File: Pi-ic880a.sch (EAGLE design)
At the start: 20 parts, among them Q1 LFXTAL016178, U1 IC880A, U2 BR24G32-3, U3 MCP79412-I/SN

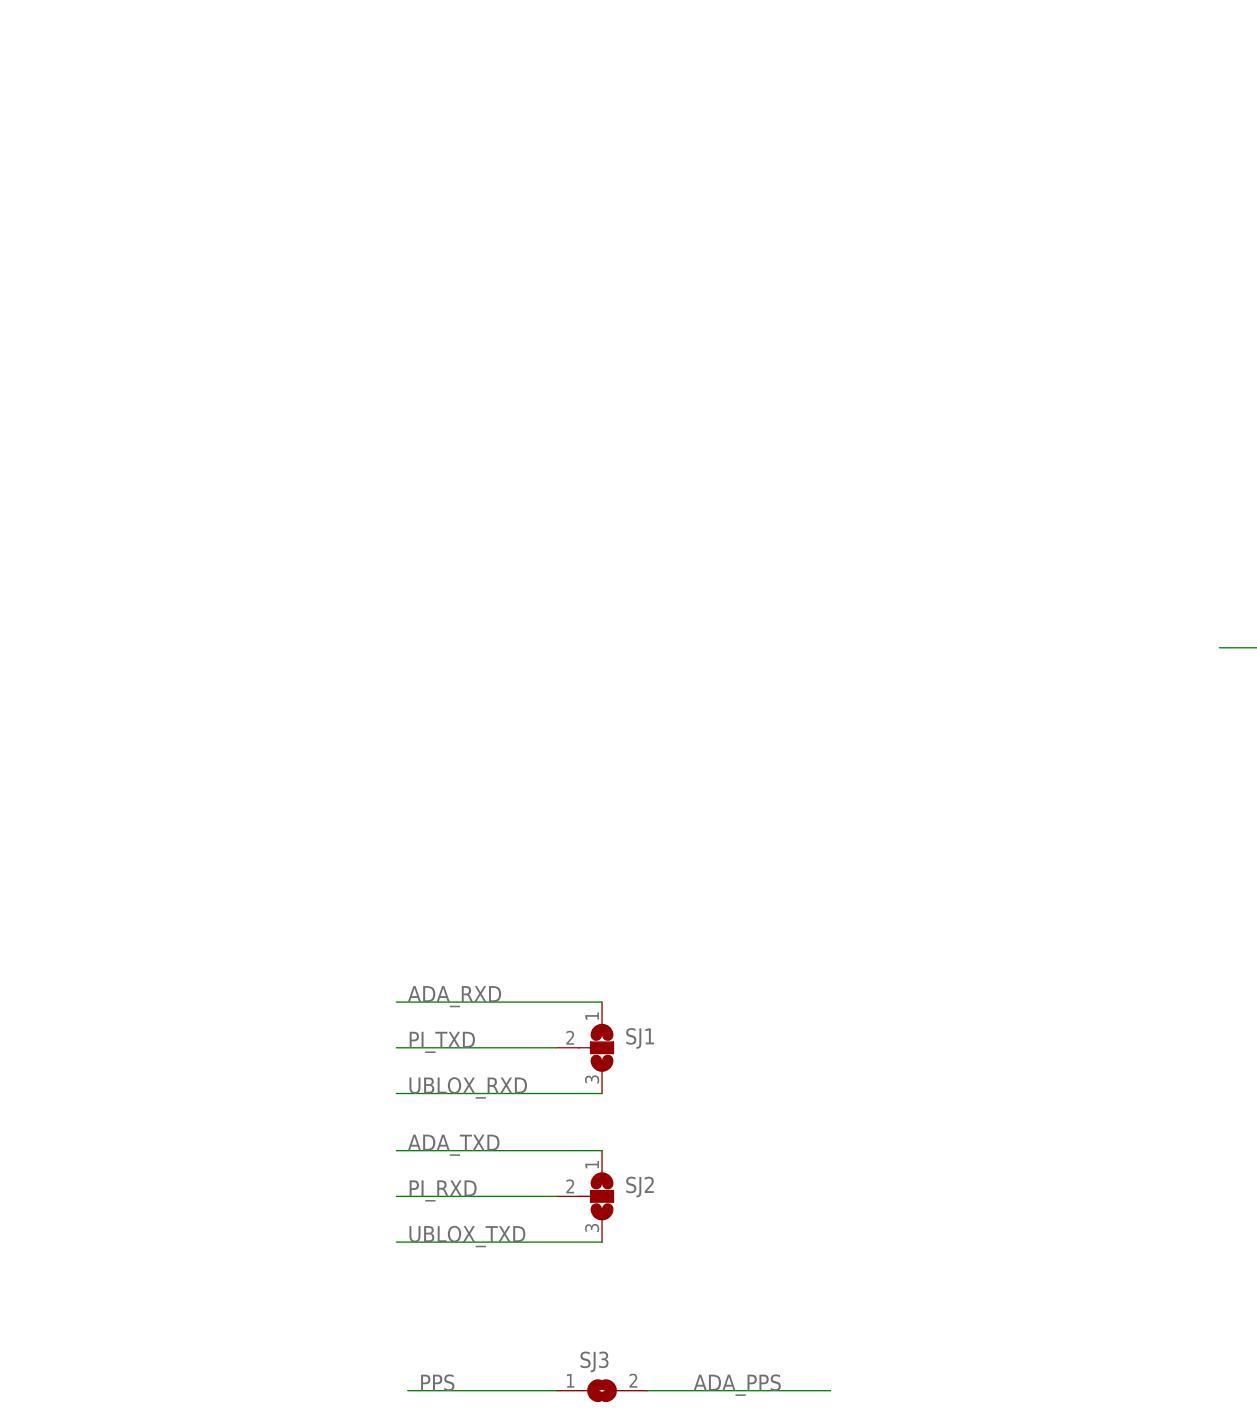
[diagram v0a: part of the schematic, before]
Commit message: Standalone version of the adafruit GPS module added
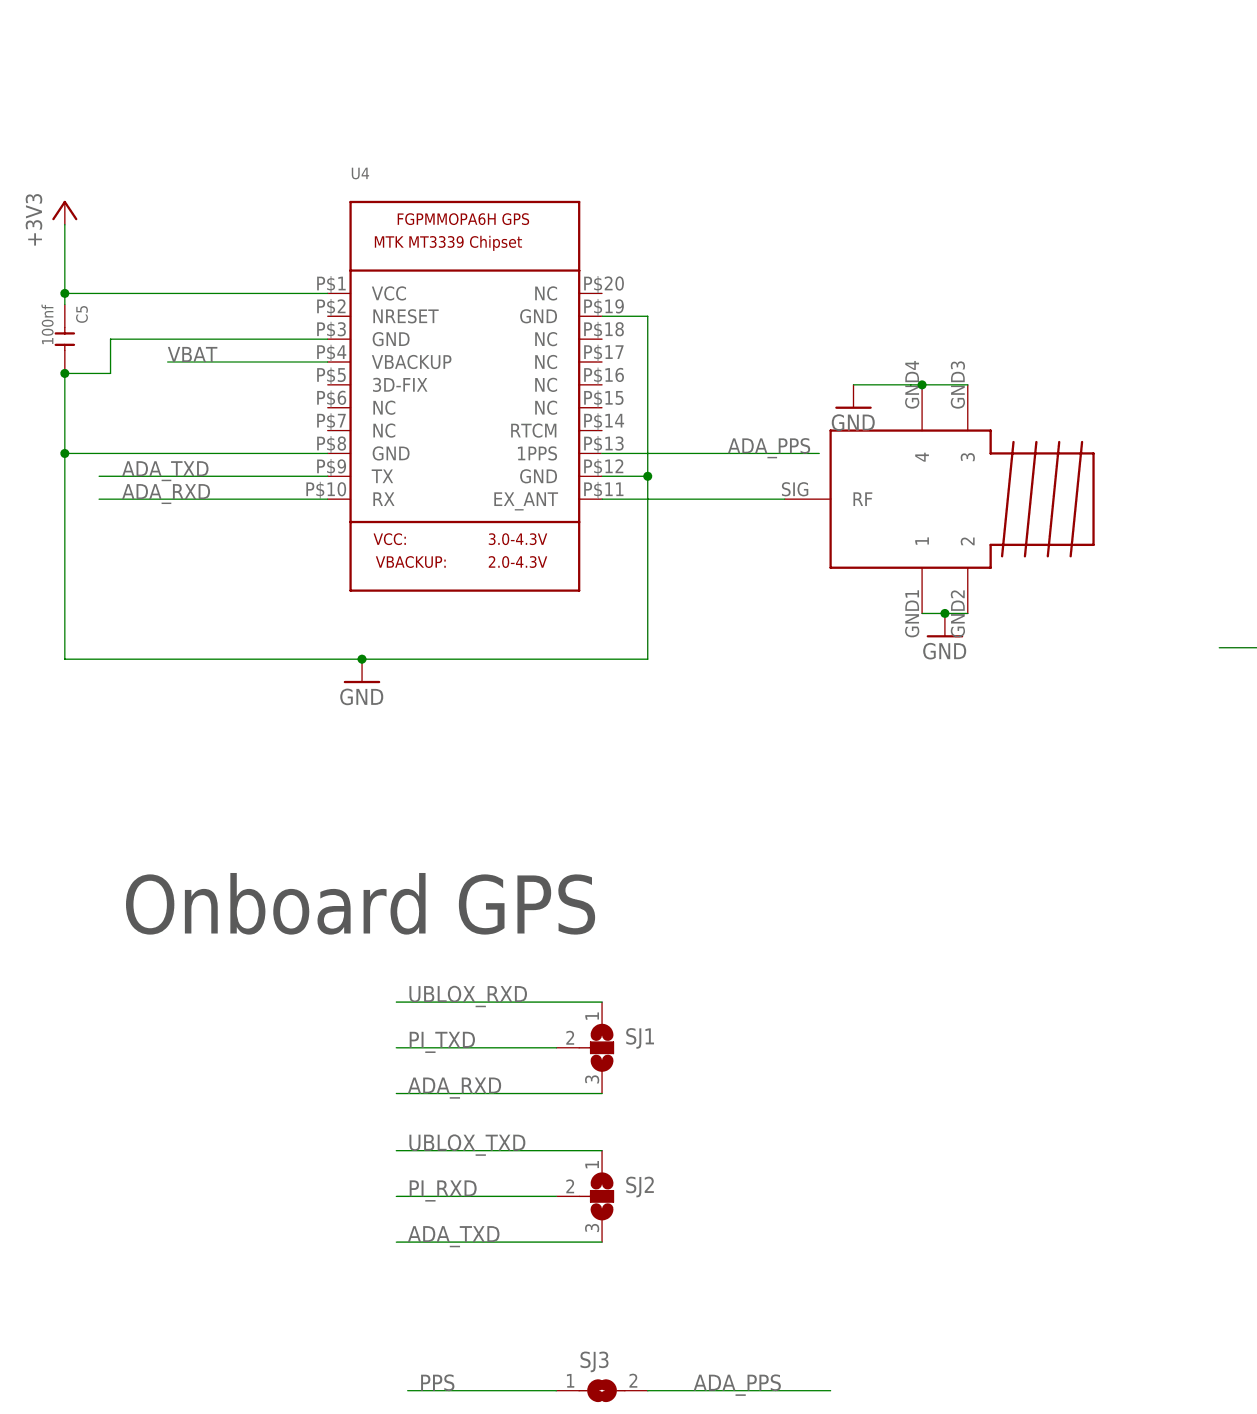
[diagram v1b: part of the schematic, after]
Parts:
- added C5: 100nf, Seeed-Capacitor-2016:CERAMIC-100NF-50V-10%-X7R(0603)
- added U$2: SMATH, fruit-parts:SMATH
- added U4: (no value), fruit-parts:GPS_FGPMMOPA6H
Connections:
- new net GPS_ANT: U$2.RF, U4.EX_ANT
- net +3V3: now also C5.1, U4.VCC
- net ADA_PPS: now also U4.1PPS
- net ADA_RXD: now also SJ1.3, U4.RX; no longer SJ1.1
- net ADA_TXD: now also SJ2.3, U4.TX; no longer SJ2.1
- net GND: now also C5.2, U$2.1, U$2.2, U$2.3, U$2.4, U4.GND@1, U4.GND@2, U4.GND@3, U4.GND@4
- net UBLOX_RXD: now also SJ1.1; no longer SJ1.3
- net UBLOX_TXD: now also SJ2.1; no longer SJ2.3
- net VBAT: now also U4.VBACKUP
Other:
- note added: "Onboard GPS"

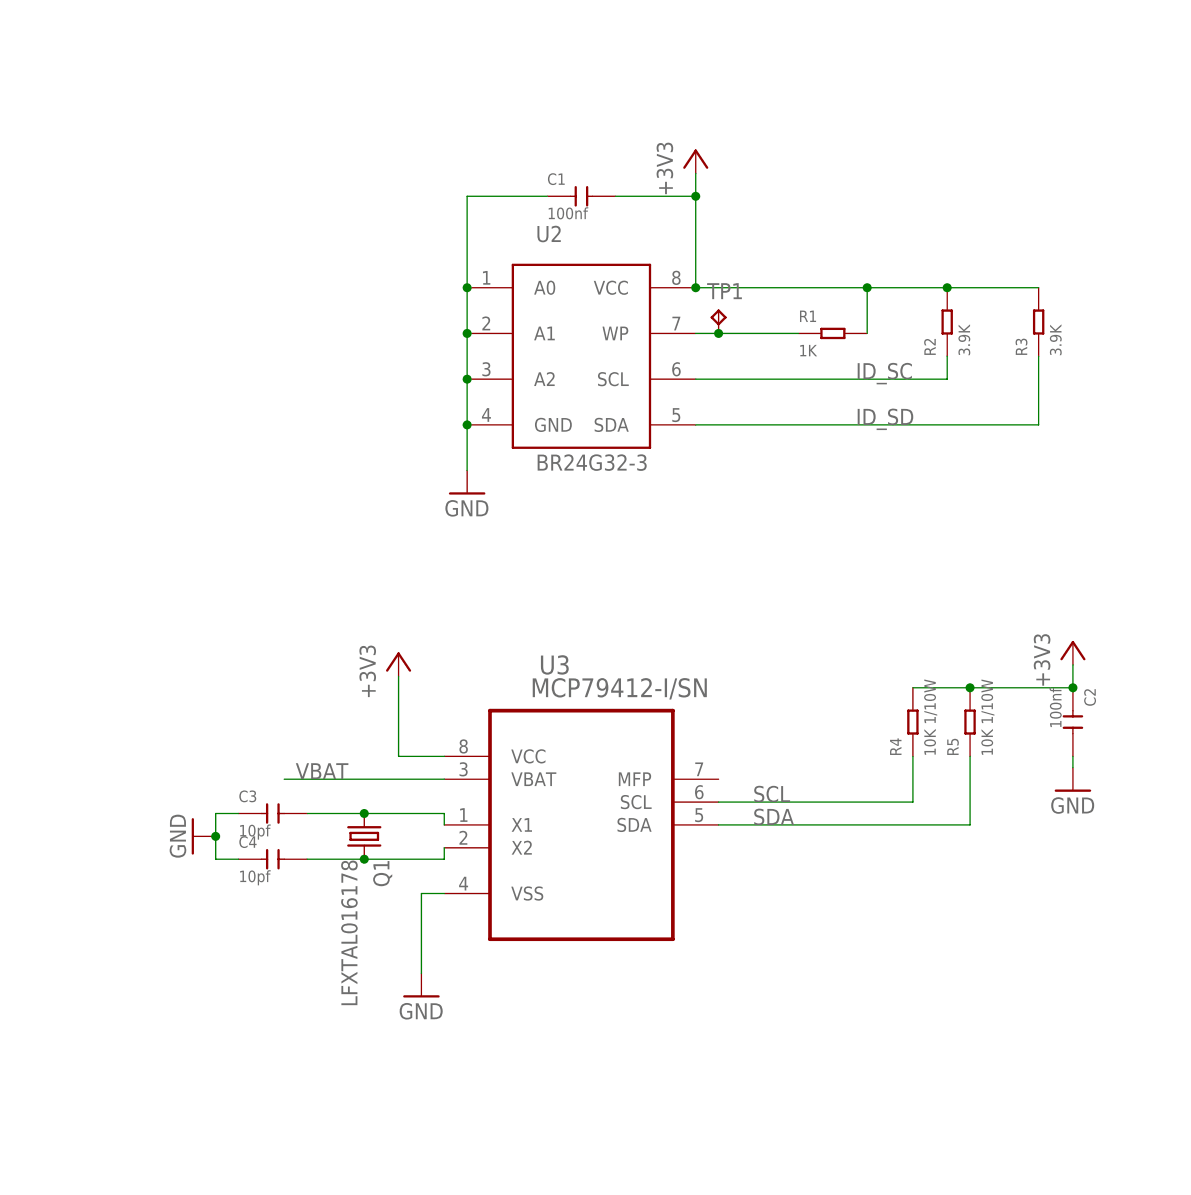
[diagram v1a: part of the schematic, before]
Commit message: Now uses ds3231 as RTC
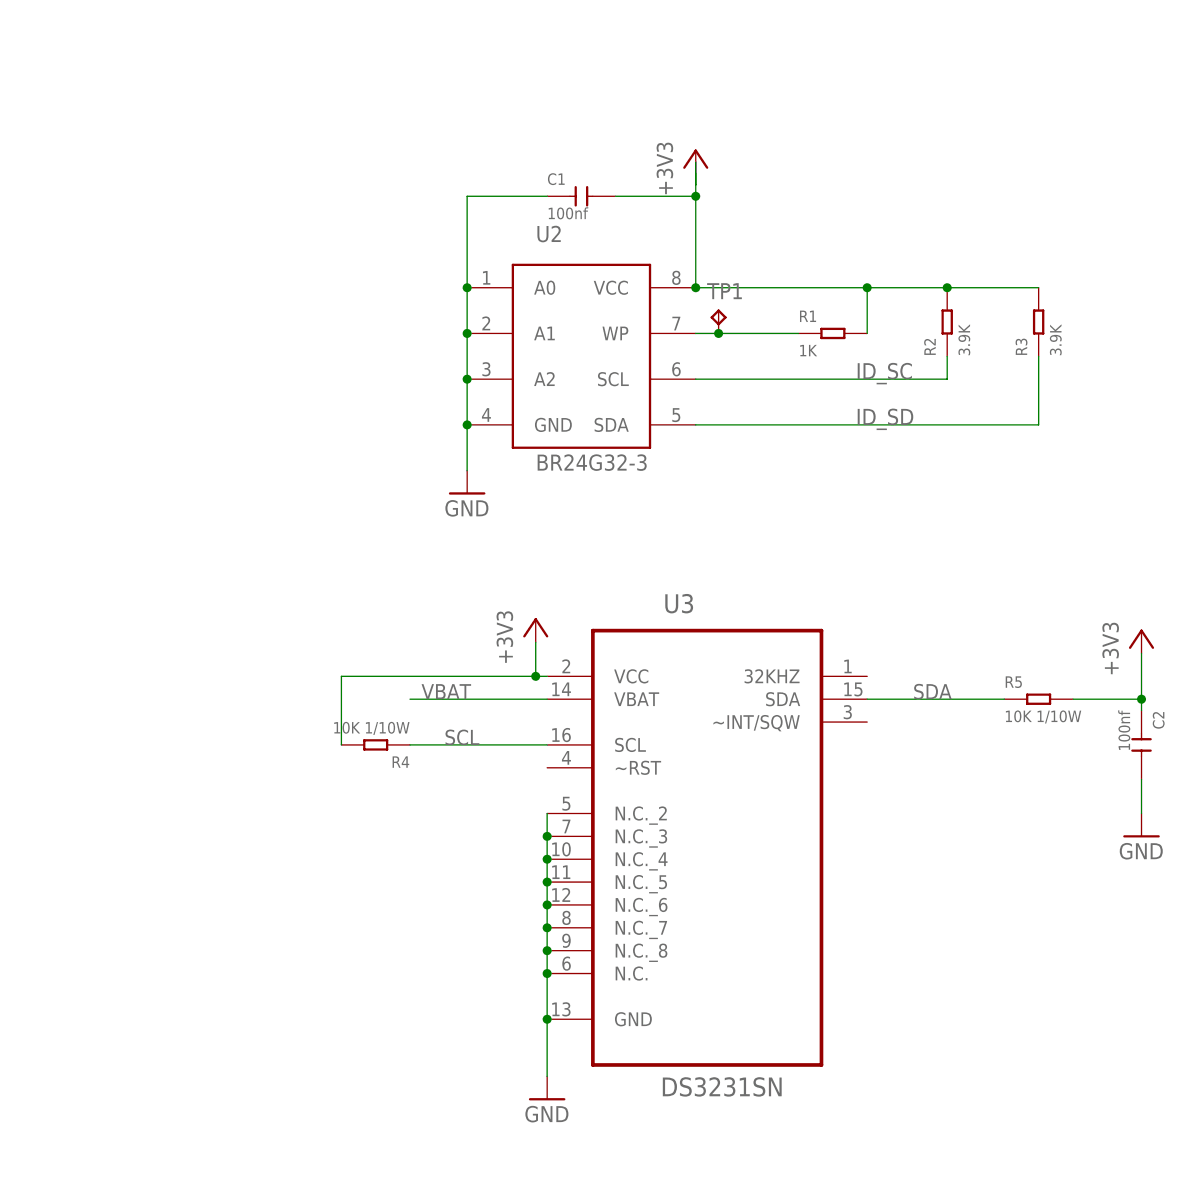
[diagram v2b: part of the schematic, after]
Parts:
- removed C3, C4: 10pf, Seeed-Capacitor-2016:CERAMIC-10PF-50V-5%-NPO(0603)
- removed Q1: LFXTAL016178, fruit-parts:LFXTAL016178
- U3: value MCP79412-I/SN -> DS3231SN; device farnell-parts:MCP79412-I/SN -> imported-parts:DS3231SN
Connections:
- removed net X1: C3.2, Q1.1, U3.X1
- removed net X2: C4.2, Q1.2, U3.X2
- net GND: now also U3.GND, U3.N.C., U3.N.C._2, U3.N.C._3, U3.N.C._4, U3.N.C._5, U3.N.C._6, U3.N.C._7, U3.N.C._8; no longer C3.1, C4.1, U3.VSS
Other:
- moved on the sheet: C2, R4, R5

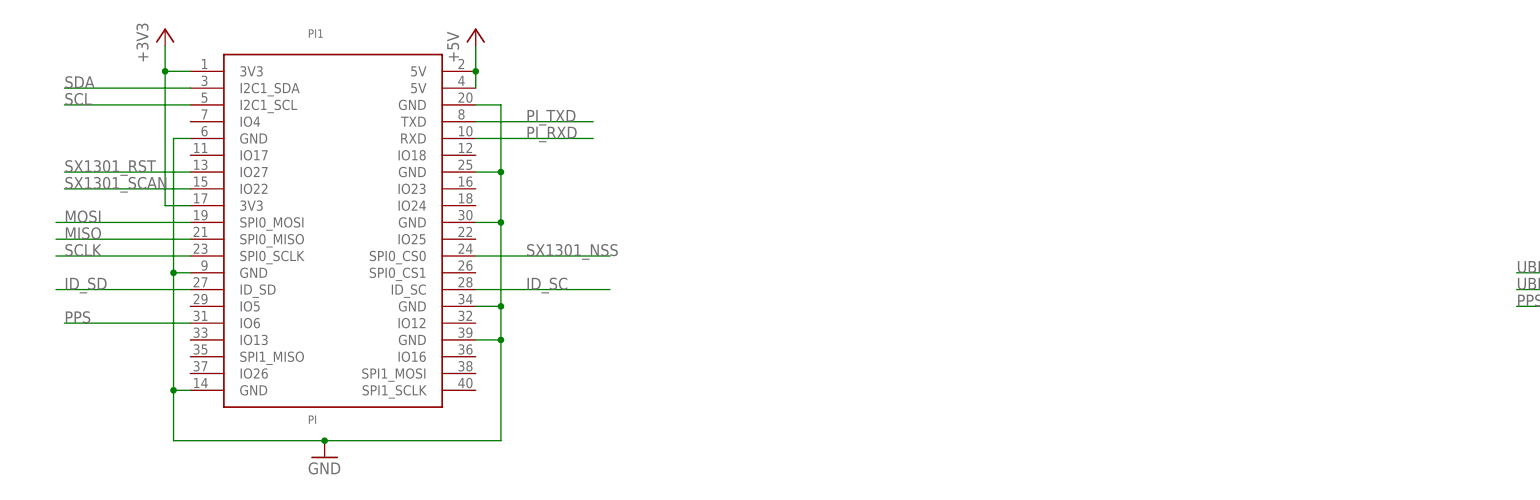
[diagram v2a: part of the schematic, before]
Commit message: DHT22 added now fully laid out and ready for final check through
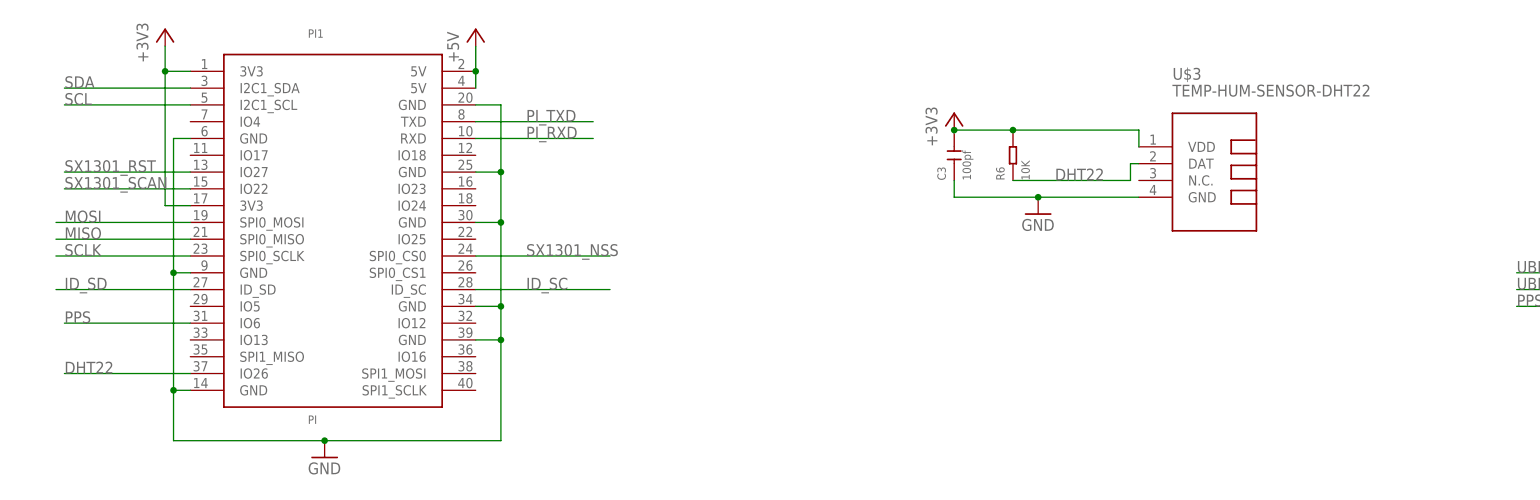
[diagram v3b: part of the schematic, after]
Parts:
- added C3: 100pf, Seeed-Capacitor:CERAMIC-100PF-50V-5%-NPO(0603)
- added R6: 10K, Seeed-Resistor:SMD-RES-10K-1%-1/10W(0603)
- added U$3: TEMP-HUM-SENSOR-DHT22, fruit-parts:TEMP-HUM-SENSOR-DHT22
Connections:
- new net DHT22: PI1.IO26, R6.1, U$3.DAT
- net +3V3: now also C3.2, R6.2, U$3.VDD
- net GND: now also C3.1, U$3.GND
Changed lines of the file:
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@@
 <?xml version="1.0" encoding="utf-8"?>
 <!DOCTYPE eagle SYSTEM "eagle.dtd">
-<eagle version="8.3.0">
+<eagle version="8.3.2">
 <drawing>
 <settings>
@@
 <part name="U3" library="imported-parts" deviceset="DS3231SN" device=""/>
 <part name="+3V2" library="supply1" library_urn="urn:adsk.eagle:library:371" deviceset="+3V3" device=""/>
+<part name="U$3" library="fruit-parts" deviceset="TEMP-HUM-SENSOR-DHT22" device=""/>
+<part name="C3" library="Seeed-Capacitor" library_urn="urn:adsk.eagle:library:464" deviceset="CERAMIC-100PF-50V-5%-NPO(0603)" device="" package3d_urn="urn:adsk.eagle:package:32378/1" value="100pf"/>
+<part name="R6" library="Seeed-Resistor" library_urn="urn:adsk.eagle:library:474" deviceset="SMD-RES-10K-1%-1/10W(0603)" device="" package3d_urn="urn:adsk.eagle:package:32791/1" value="10K"/>
+<part name="+3V6" library="supply1" library_urn="urn:adsk.eagle:library:371" deviceset="+3V3" device=""/>
+<part name="GND5" library="supply1" library_urn="urn:adsk.eagle:library:371" deviceset="GND" device=""/>
 </parts>
 <sheets>
@@
 <instance part="U3" gate="A" x="321.31" y="66.04"/>
 <instance part="+3V2" gate="G$1" x="302.26" y="87.63"/>
+<instance part="U$3" gate="G$1" x="212.09" y="229.87"/>
+<instance part="C3" gate="G$1" x="171.45" y="233.68" rot="R90"/>
+<instance part="R6" gate="G$1" x="180.34" y="233.68" rot="R90"/>
+<instance part="+3V6" gate="G$1" x="171.45" y="240.03"/>
+<instance part="GND5" gate="1" x="184.15" y="224.79"/>
 </instances>
 <busses>
@@
 <junction x="303.53" y="43.18"/>
 </segment>
+<segment>
+<pinref part="U$3" gate="G$1" pin="GND"/>
+<pinref part="C3" gate="G$1" pin="1"/>
+<wire x1="199.39" y1="227.33" x2="184.15" y2="227.33" width="0.1524" layer="91"/>
+<wire x1="184.15" y1="227.33" x2="171.45" y2="227.33" width="0.1524" layer="91"/>
+<wire x1="171.45" y1="227.33" x2="171.45" y2="229.87" width="0.1524" layer="91"/>
+<pinref part="GND5" gate="1" pin="GND"/>
+<junction x="184.15" y="227.33"/>
+</segment>
 </net>
 <net name="UBLOX_TXD" class="0">
@@
 <junction x="369.57" y="78.74"/>
 </segment>
+<segment>
+<pinref part="C3" gate="G$1" pin="2"/>
+<pinref part="R6" gate="G$1" pin="2"/>
+<wire x1="171.45" y1="237.49" x2="180.34" y2="237.49" width="0.1524" layer="91"/>
+<pinref part="U$3" gate="G$1" pin="VDD"/>
+<wire x1="180.34" y1="237.49" x2="199.39" y2="237.49" width="0.1524" layer="91"/>
+<wire x1="199.39" y1="237.49" x2="199.39" y2="234.95" width="0.1524" layer="91"/>
+<junction x="180.34" y="237.49"/>
+<pinref part="+3V6" gate="G$1" pin="+3V3"/>
+<junction x="171.45" y="237.49"/>
+</segment>
 </net>
 <net name="ID_SC" class="0">
@@
 </segment>
 </net>
+<net name="DHT22" class="0">
+<segment>
+<pinref part="U$3" gate="G$1" pin="DAT"/>
+<wire x1="199.39" y1="232.41" x2="198.12" y2="232.41" width="0.1524" layer="91"/>
+<wire x1="198.12" y1="232.41" x2="198.12" y2="229.87" width="0.1524" layer="91"/>
+<pinref part="R6" gate="G$1" pin="1"/>
+<wire x1="198.12" y1="229.87" x2="180.34" y2="229.87" width="0.1524" layer="91"/>
+<label x="186.69" y="229.87" size="1.778" layer="95"/>
+</segment>
+<segment>
+<pinref part="PI1" gate="G$1" pin="IO26"/>
+<wire x1="55.88" y1="200.66" x2="36.83" y2="200.66" width="0.1524" layer="91"/>
+<label x="36.83" y="200.66" size="1.778" layer="95"/>
+</segment>
+</net>
